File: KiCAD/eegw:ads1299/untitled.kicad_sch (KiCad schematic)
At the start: 87 parts, among them J8 Conn_01x10, U2 INA128U, U3 INA128U, U4 INA128U, U5 INA128U, U6 INA128U, U7 INA128U, U8 INA128U, U9 INA128U

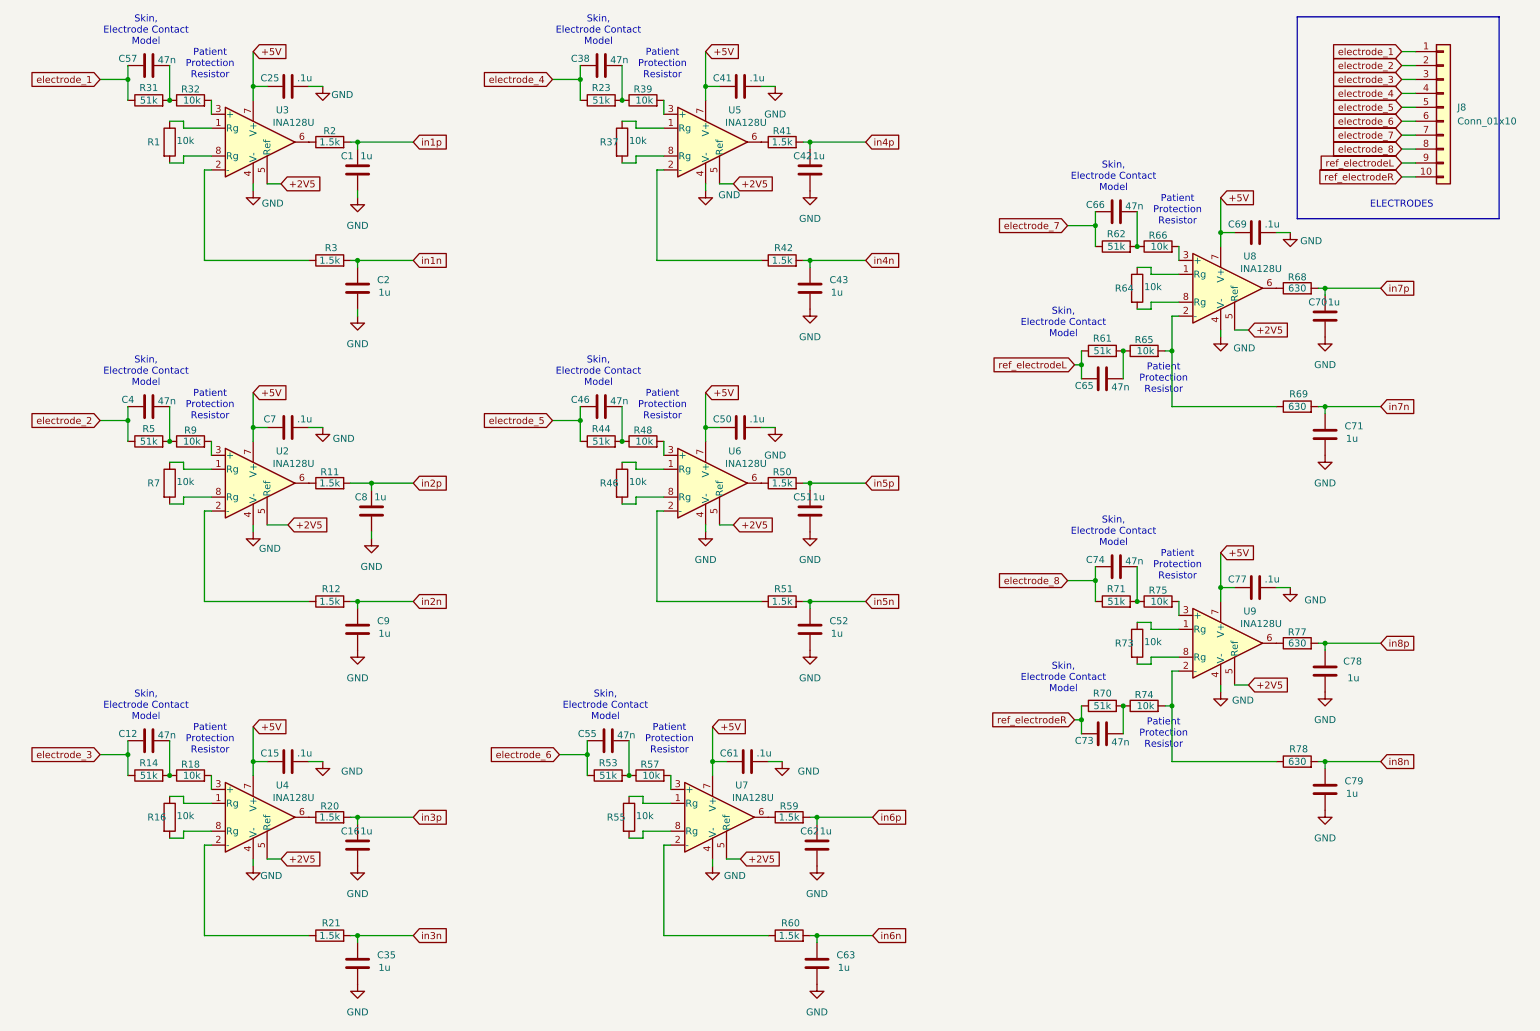
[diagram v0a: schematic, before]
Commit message: updated kicad renumbered
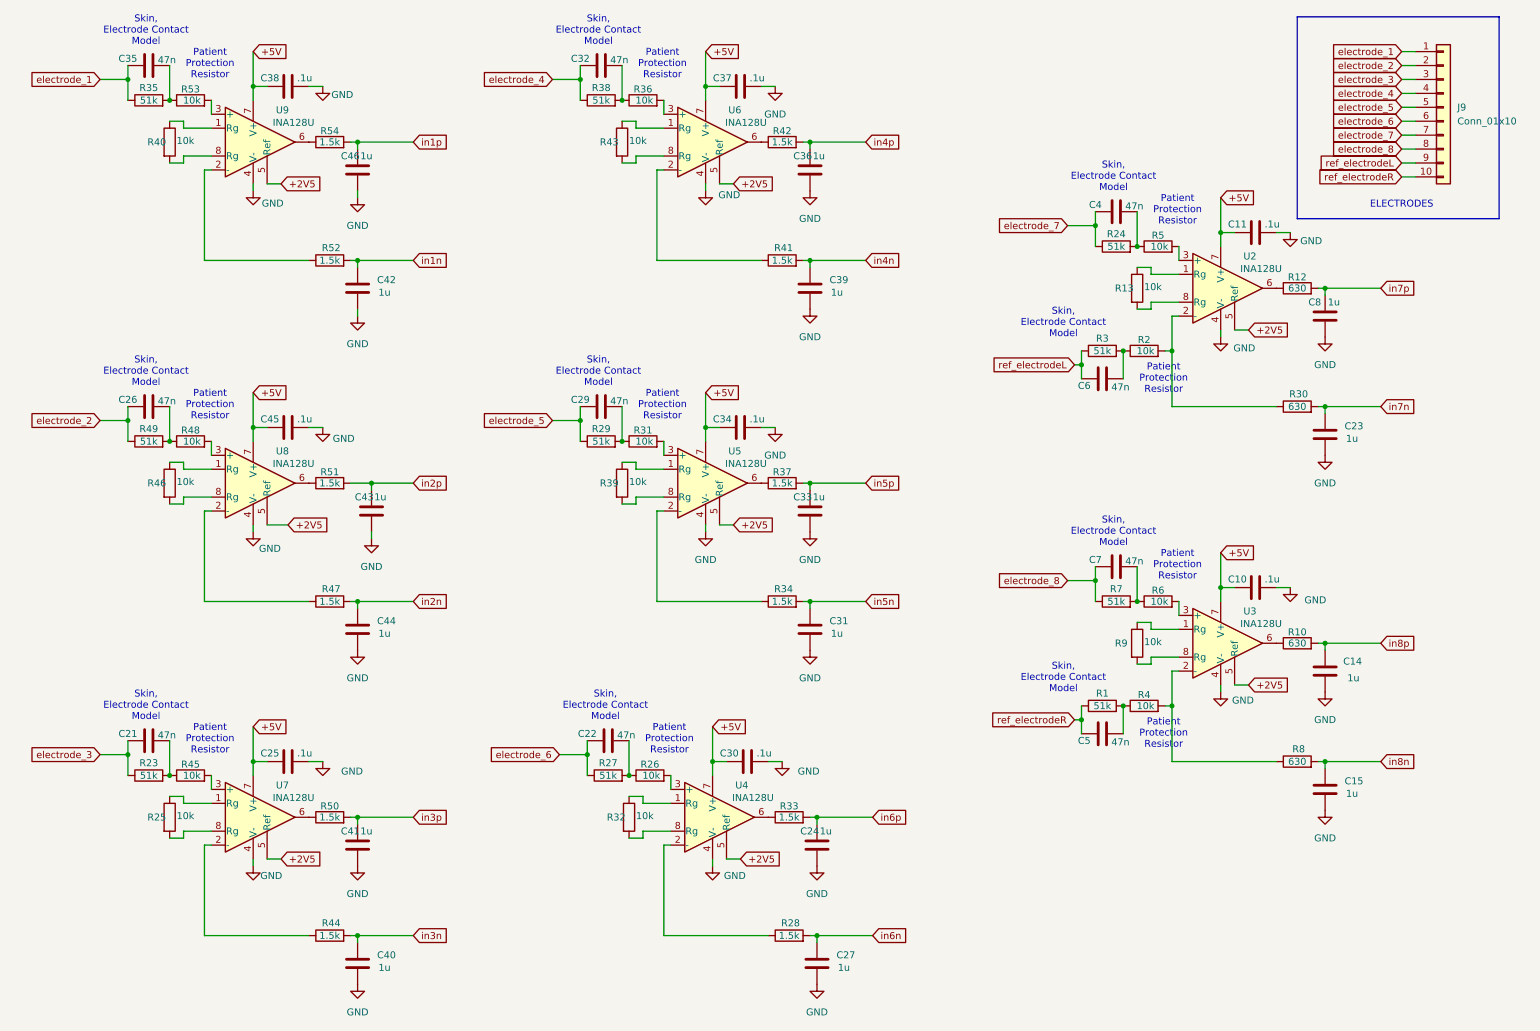
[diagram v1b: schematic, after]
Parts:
- renumbered C77 to C10, C69 to C11, C78 to C14, C79 to C15, C12 to C21, C55 to C22, C71 to C23, C62 to C24, C15 to C25, C4 to C26, C63 to C27, C46 to C29, C61 to C30, C52 to C31, C38 to C32, C51 to C33, C50 to C34, C57 to C35, C42 to C36, C41 to C37, C25 to C38, C43 to C39, C66 to C4, C35 to C40, C16 to C41, C2 to C42, C8 to C43, C9 to C44, C7 to C45, C1 to C46, C73 to C5, C65 to C6, C74 to C7, C70 to C8, J8 to J9, R70 to R1, R77 to R10, R68 to R12, R64 to R13, R65 to R2, R14 to R23, R62 to R24, R16 to R25, R57 to R26, R53 to R27, R60 to R28, R44 to R29, R61 to R3, R69 to R30, R48 to R31, R55 to R32, R59 to R33, R51 to R34, R31 to R35, R39 to R36, R50 to R37, R23 to R38, R46 to R39, R74 to R4, R1 to R40, R42 to R41, R41 to R42, R37 to R43, R21 to R44, R18 to R45, R7 to R46, R12 to R47, R9 to R48, R5 to R49, R66 to R5, R20 to R50, R11 to R51, R3 to R52, R32 to R53, R2 to R54, R75 to R6, R71 to R7, R78 to R8, R73 to R9, U8 to U2, U9 to U3, U7 to U4, U6 to U5, U5 to U6, U4 to U7, U2 to U8, U3 to U9
